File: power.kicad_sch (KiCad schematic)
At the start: 70 parts, among them U801 TPS566231P, U802 TPS566231P, U803 TPS566231P, U804 TPS566231P

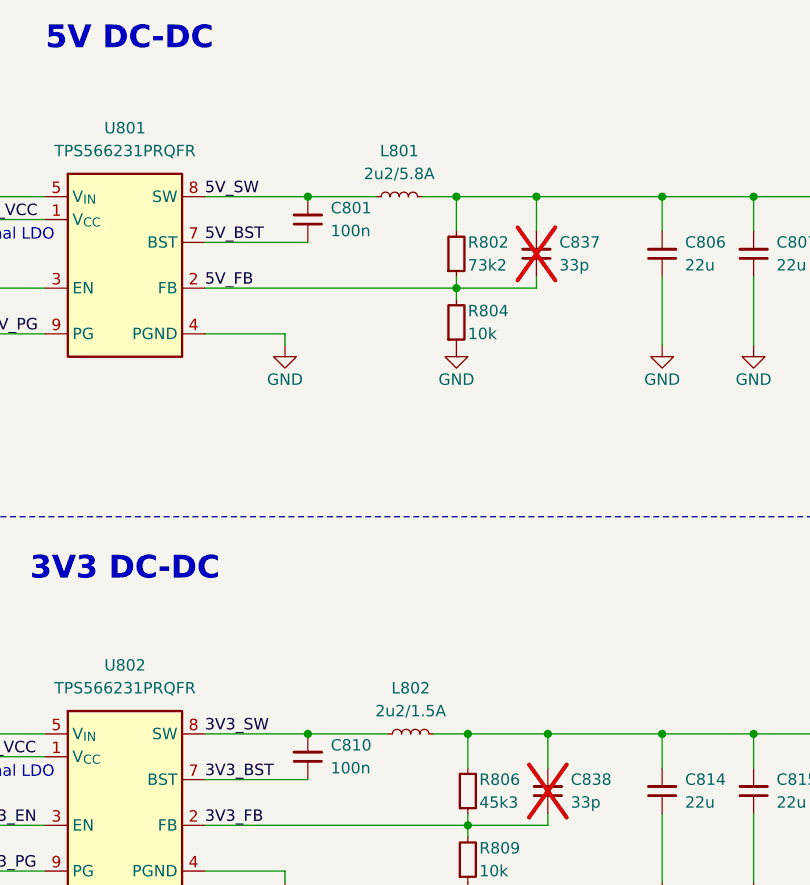
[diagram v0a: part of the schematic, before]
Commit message: [#100501] Change 5V & 3V3 DCDC inductors for SRP3212A-2R2M
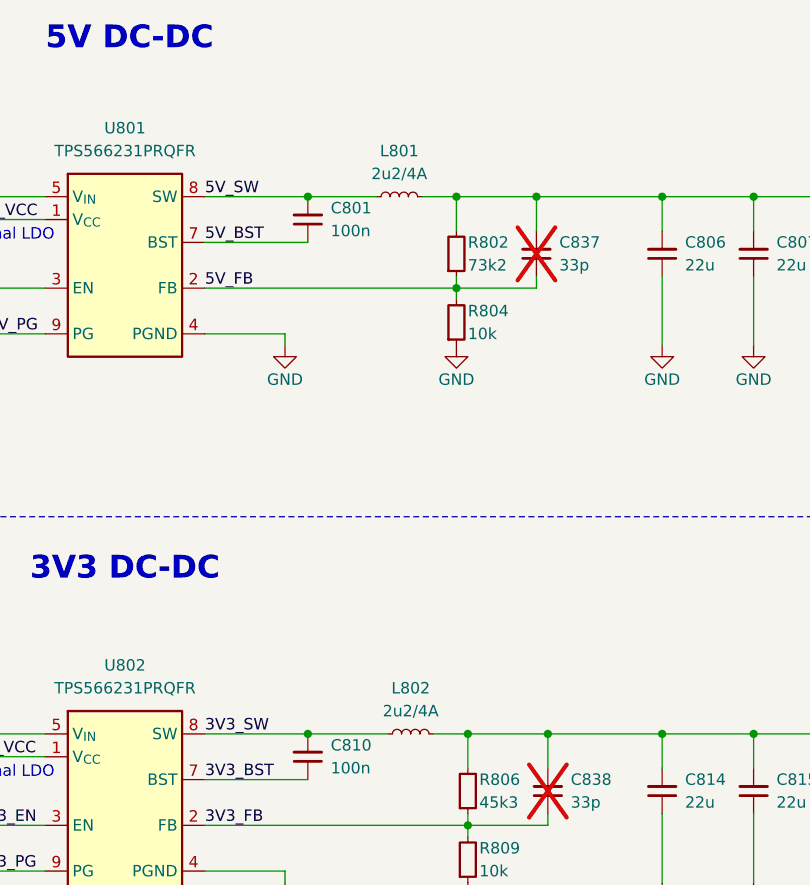
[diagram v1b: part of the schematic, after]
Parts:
- L801: value L_2u2_5.8A_WE-PMFI-35329222 -> L_2u2_4A_Bourns-SRP3212A; footprint antmicro-footprints:L_WE-PMFI-353220 -> antmicro-footprints:L_Bourns-SRP3212A; symbol antmicroFixedInductors:L_2u2_5.8A_WE-PMFI-35329222 -> antmicroFixedInductors:L_2u2_4A_Bourns-SRP3212A; IMax 5.8A -> 4 A; ISat 7.8A -> 4.8 A; MPN 74479335329222 -> SRP3212A-2R2M; Manufacturer Würth Elektronik -> Bourns; Size 3.5x3.2x2.0 -> 3.2x2.5; Val 2u2/5.8A -> 2u2/4A
- L802: value L_2u2_1.5A_0806 -> L_2u2_4A_Bourns-SRP3212A; footprint antmicro-footprints:L_0806_2016Metric -> antmicro-footprints:L_Bourns-SRP3212A; symbol antmicroFixedInductors:L_2u2_1.5A_0806 -> antmicroFixedInductors:L_2u2_4A_Bourns-SRP3212A; IMax (none) -> 4 A; ISat (none) -> 4.8 A; Imax 1.5A -> (none); Isat 1.2A -> (none); MPN 1285AS-H-2R2M=P2 -> SRP3212A-2R2M; Manufacturer Murata -> Bourns; Size 2.0x1.6 -> 3.2x2.5; Val 2u2/1.5A -> 2u2/4A
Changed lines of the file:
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@@
 	)
 	(symbol
-		(lib_id "antmicroFixedInductors:L_2u2_5.8A_WE-PMFI-35329222")
+		(lib_id "antmicroFixedInductors:L_2u2_4A_Bourns-SRP3212A")
 		(at 233.68 40.64 0)
 		(unit 1)
@@
 			)
 		)
-		(property "Value" "L_2u2_5.8A_WE-PMFI-35329222"
+		(property "Value" "L_2u2_4A_Bourns-SRP3212A"
 			(at 247.65 43.18 0)
 			(hide yes)
@@
 			)
 		)
-		(property "Footprint" "antmicro-footprints:L_WE-PMFI-353220"
+		(property "Footprint" "antmicro-footprints:L_Bourns-SRP3212A"
 			(at 247.65 48.26 0)
 			(hide yes)
@@
 			)
 		)
-		(property "Datasheet" "https://www.we-online.com/components/products/datasheet/74479335329222.pdf"
+		(property "Datasheet" "https://bourns.com/docs/product-datasheets/srp3212a.pdf?sfvrsn=7a275df6_6"
 			(at 247.65 50.8 0)
 			(hide yes)
@@
 			)
 		)
-		(property "Description" "Power Inductors - SMD WE-PMFI 2.2 uH 5.8 A 40 mOhms AEC-Q200"
+		(property "Description" "Power Inductor (SMD), 2.2 µH, 4 A, Shielded, 4.8 A, SRP3212 Series"
 			(at 247.65 71.12 0)
 			(hide yes)
@@
 			)
 		)
-		(property "Val" "2u2/5.8A"
+		(property "Val" "2u2/4A"
 			(at 236.22 38.1 0)
 			(show_name no)
@@
 			)
 		)
-		(property "Manufacturer" "Würth Elektronik"
+		(property "Manufacturer" "Bourns"
 			(at 247.65 53.34 0)
 			(hide yes)
@@
 			)
 		)
-		(property "MPN" "74479335329222"
+		(property "MPN" "SRP3212A-2R2M "
 			(at 247.65 55.88 0)
 			(hide yes)
@@
 			)
 		)
-		(property "ISat" "7.8A"
-			(at 247.65 58.42 0)
+		(property "ISat" "4.8 A"
+			(at 247.65 57.15 0)
 			(hide yes)
 			(show_name no)
@@
 					(size 1.27 1.27)
 				)
-				(justify left bottom)
+				(justify left)
 			)
 		)
-		(property "IMax" "5.8A"
+		(property "IMax" "4 A"
 			(at 247.65 60.96 0)
 			(hide yes)
@@
 			)
 		)
-		(property "Size" "3.5x3.2x2.0"
+		(property "Size" "3.2x2.5"
 			(at 247.65 63.5 0)
 			(hide yes)
@@
 	)
 	(symbol
-		(lib_id "antmicroFixedInductors:L_2u2_1.5A_0806")
+		(lib_id "antmicroFixedInductors:L_2u2_4A_Bourns-SRP3212A")
 		(at 234.95 100.33 0)
 		(unit 1)
@@
 			)
 		)
-		(property "Value" "L_2u2_1.5A_0806"
+		(property "Value" "L_2u2_4A_Bourns-SRP3212A"
 			(at 248.92 102.87 0)
 			(hide yes)
@@
 			)
 		)
-		(property "Footprint" "antmicro-footprints:L_0806_2016Metric"
+		(property "Footprint" "antmicro-footprints:L_Bourns-SRP3212A"
 			(at 248.92 107.95 0)
 			(hide yes)
@@
 			)
 		)
-		(property "Datasheet" "https://search.murata.co.jp/Ceramy/image/img/P02/J(E)TE243A-0011.pdf"
+		(property "Datasheet" "https://bourns.com/docs/product-datasheets/srp3212a.pdf?sfvrsn=7a275df6_6"
 			(at 248.92 110.49 0)
 			(hide yes)
@@
 			)
 		)
-		(property "Description" "Power Inductor (SMD), 2.2 µH, 1.2 A, Shielded, 1.5 A, DFE201610C"
+		(property "Description" "Power Inductor (SMD), 2.2 µH, 4 A, Shielded, 4.8 A, SRP3212 Series"
 			(at 248.92 130.81 0)
 			(hide yes)
@@
 			)
 		)
-		(property "Val" "2u2/1.5A"
+		(property "Val" "2u2/4A"
 			(at 237.49 97.79 0)
 			(show_name no)
@@
 				(font
 					(size 1.27 1.27)
+					(thickness 0.15)
 				)
 			)
 		)
-		(property "Manufacturer" "Murata"
+		(property "Manufacturer" "Bourns"
 			(at 248.92 113.03 0)
 			(hide yes)
@@
 				(font
 					(size 1.27 1.27)
+					(thickness 0.15)
 				)
 				(justify left bottom)
 			)
 		)
-		(property "MPN" "1285AS-H-2R2M=P2"
+		(property "MPN" "SRP3212A-2R2M "
 			(at 248.92 115.57 0)
 			(hide yes)
@@
 				(font
 					(size 1.27 1.27)
+					(thickness 0.15)
 				)
 				(justify left bottom)
 			)
 		)
-		(property "ISat" ""
+		(property "ISat" "4.8 A"
 			(at 248.92 116.84 0)
 			(hide yes)
@@
 			)
 		)
-		(property "Isat" "1.2A"
-			(at 248.92 118.11 0)
-			(hide yes)
-			(show_name no)
-			(do_not_autoplace no)
-			(effects
-				(font
-					(size 1.27 1.27)
-				)
-				(justify left bottom)
-			)
-		)
-		(property "IMax" ""
+		(property "IMax" "4 A"
 			(at 248.92 120.65 0)
 			(hide yes)
@@
 			)
 		)
-		(property "Imax" "1.5A"
-			(at 248.92 120.65 0)
-			(hide yes)
-			(show_name no)
-			(do_not_autoplace no)
-			(effects
-				(font
-					(size 1.27 1.27)
-				)
-				(justify left bottom)
-			)
-		)
-		(property "Size" "2.0x1.6"
+		(property "Size" "3.2x2.5"
 			(at 248.92 123.19 0)
 			(hide yes)
@@
 				(font
 					(size 1.27 1.27)
+					(thickness 0.15)
 				)
 				(justify left bottom)
@@
 				(font
 					(size 1.27 1.27)
+					(thickness 0.15)
 				)
 				(justify left bottom)
@@
 				(font
 					(size 1.27 1.27)
+					(thickness 0.15)
 				)
 				(justify left bottom)

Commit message: [#100501] Reannotate schematic
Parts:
- renumbered C801 to C29, C802 to C30, C803 to C31, C804 to C32, C805 to C33, C837 to C34, C806 to C35, C807 to C36, C808 to C37, C809 to C38, C810 to C39, C811 to C40, C812 to C41, C813 to C42, C838 to C43, C814 to C44, C815 to C45, C816 to C46, C817 to C47, C818 to C48, C819 to C49, C820 to C50, C821 to C51, C822 to C52, C839 to C53, C823 to C54, C824 to C55, C825 to C56, C826 to C57, C827 to C58, C828 to C59, C829 to C60, C830 to C61, C831 to C62, C832 to C63, C840 to C64, C833 to C65, C834 to C66, C835 to C67, C836 to C68, L801 to L1, L802 to L2, L803 to L3, L804 to L4, R801 to R73, R821 to R74, R803 to R75, R802 to R76, R822 to R77, R804 to R78, R805 to R79, R806 to R80, R807 to R81, R808 to R82, R809 to R83, R810 to R84, R811 to R85, R812 to R86, R813 to R87, R814 to R88, R815 to R89, R816 to R90, R817 to R91, R818 to R92, R819 to R93, R820 to R94, U801 to U4, U802 to U5, U803 to U6, U804 to U7

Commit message: [#100501] Correct +3V3_HPM_FRU connection
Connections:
- net +1V05: no longer R88.1
- net +3V3: now also R88.1

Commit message: [#100501] Change 1V2 and 1V05 DCDC inductors and add current draw assumptions
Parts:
- L3, L4: value L_2u2_1.5A_0806 -> L_1u_2.6A_0806; symbol antmicroFixedInductors:L_2u2_1.5A_0806 -> antmicroFixedInductors:L_1u_2.6A_0806; IMax (none) -> 2.6 A; ISat (none) -> 2.9 A; Imax 1.5A -> (none); Isat 1.2A -> (none); MPN 1285AS-H-2R2M=P2 -> SRP2010-1R0M; Manufacturer Murata -> Bourns; Val 2u2/1.5A -> 1u/2.6A
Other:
- note added: "1V05 @ 1A"
- note added: "1V2 @ 0.5A"
- note added: "3V3 @ 1A"
- note added: "5V @ 3.5A"
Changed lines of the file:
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@@
 		)
 	)
+	(text "3V3 @ 1A"
+		(exclude_from_sim no)
+		(at 267.462 97.536 0)
+		(effects
+			(font
+				(size 1.27 1.27)
+			)
+		)
+	)
+	(text "5V @ 3.5A"
+		(exclude_from_sim no)
+		(at 268.986 37.846 0)
+		(effects
+			(font
+				(size 1.27 1.27)
+			)
+		)
+	)
 	(text "V_{OUT} = 0.6 x (1 + R_{H}/R_{L}) [V]"
 		(exclude_from_sim no)
@@
 		)
 	)
+	(text "1V2 @ 0.5A"
+		(exclude_from_sim no)
+		(at 268.224 212.09 0)
+		(effects
+			(font
+				(size 1.27 1.27)
+			)
+		)
+	)
 	(text "1V05 DC-DC"
 		(exclude_from_sim no)
@@
 		)
 	)
+	(text "1V05 @ 1A"
+		(exclude_from_sim no)
+		(at 266.954 151.384 0)
+		(effects
+			(font
+				(size 1.27 1.27)
+			)
+		)
+	)
 	(text "VCC_SCM_HPM_FRU \n+3V3 +/- 5%\n0.627W"
 		(exclude_from_sim no)
@@
 	)
 	(symbol
-		(lib_id "antmicroFixedInductors:L_2u2_1.5A_0806")
+		(lib_id "antmicroFixedInductors:L_1u_2.6A_0806")
 		(at 237.49 214.63 0)
 		(unit 1)
@@
 			)
 		)
-		(property "Value" "L_2u2_1.5A_0806"
+		(property "Value" "L_1u_2.6A_0806"
 			(at 251.46 217.17 0)
 			(hide yes)
@@
 			)
 		)
-		(property "Datasheet" "https://search.murata.co.jp/Ceramy/image/img/P02/J(E)TE243A-0011.pdf"
+		(property "Datasheet" "https://www.bourns.com/docs/Product-Datasheets/SRP2010.pdf"
 			(at 251.46 224.79 0)
 			(hide yes)
@@
 			)
 		)
-		(property "Description" "Power Inductor (SMD), 2.2 µH, 1.2 A, Shielded, 1.5 A, DFE201610C"
+		(property "Description" "Wirewound Inductor, 1 µH, 0.072 ohm, 2.6 A, SRP2010"
 			(at 251.46 245.11 0)
 			(hide yes)
@@
 			)
 		)
-		(property "Val" "2u2/1.5A"
+		(property "Val" "1u/2.6A"
 			(at 240.03 212.09 0)
 			(show_name no)
@@
 				(font
 					(size 1.27 1.27)
+					(thickness 0.15)
 				)
 			)
 		)
-		(property "Manufacturer" "Murata"
+		(property "Manufacturer" "Bourns"
 			(at 251.46 227.33 0)
 			(hide yes)
@@
 				(font
 					(size 1.27 1.27)
+					(thickness 0.15)
 				)
 				(justify left bottom)
 			)
 		)
-		(property "MPN" "1285AS-H-2R2M=P2"
+		(property "MPN" "SRP2010-1R0M"
 			(at 251.46 229.87 0)
 			(hide yes)
@@
 				(font
 					(size 1.27 1.27)
+					(thickness 0.15)
 				)
 				(justify left bottom)
 			)
 		)
-		(property "ISat" ""
+		(property "ISat" "2.9 A"
 			(at 251.46 231.14 0)
 			(hide yes)
@@
 			)
 		)
-		(property "Isat" "1.2A"
-			(at 251.46 232.41 0)
-			(hide yes)
-			(show_name no)
-			(do_not_autoplace no)
-			(effects
-				(font
-					(size 1.27 1.27)
-				)
-				(justify left bottom)
-			)
-		)
-		(property "IMax" ""
+		(property "IMax" "2.6 A"
 			(at 251.46 234.95 0)
 			(hide yes)
@@
 			)
 		)
-		(property "Imax" "1.5A"
-			(at 251.46 234.95 0)
-			(hide yes)
-			(show_name no)
-			(do_not_autoplace no)
-			(effects
-				(font
-					(size 1.27 1.27)
-				)
-				(justify left bottom)
-			)
-		)
 		(property "Size" "2.0x1.6"
 			(at 251.46 237.49 0)
@@
 				(font
 					(size 1.27 1.27)
+					(thickness 0.15)
 				)
 				(justify left bottom)
@@
 				(font
 					(size 1.27 1.27)
+					(thickness 0.15)
 				)
 				(justify left bottom)
@@
 				(font
 					(size 1.27 1.27)
+					(thickness 0.15)
 				)
 				(justify left bottom)
@@
 	)
 	(symbol
-		(lib_id "antmicroFixedInductors:L_2u2_1.5A_0806")
+		(lib_id "antmicroFixedInductors:L_1u_2.6A_0806")
 		(at 237.49 153.67 0)
 		(unit 1)
@@
 			)
 		)
-		(property "Value" "L_2u2_1.5A_0806"
+		(property "Value" "L_1u_2.6A_0806"
 			(at 251.46 156.21 0)
 			(hide yes)
@@
 			)
 		)
-		(property "Datasheet" "https://search.murata.co.jp/Ceramy/image/img/P02/J(E)TE243A-0011.pdf"
+		(property "Datasheet" "https://www.bourns.com/docs/Product-Datasheets/SRP2010.pdf"
 			(at 251.46 163.83 0)
 			(hide yes)
@@
 			)
 		)
-		(property "Description" "Power Inductor (SMD), 2.2 µH, 1.2 A, Shielded, 1.5 A, DFE201610C"
+		(property "Description" "Wirewound Inductor, 1 µH, 0.072 ohm, 2.6 A, SRP2010"
 			(at 251.46 184.15 0)
 			(hide yes)
@@
 			)
 		)
-		(property "Val" "2u2/1.5A"
+		(property "Val" "1u/2.6A"
 			(at 240.03 151.13 0)
 			(show_name no)
@@
 				(font
 					(size 1.27 1.27)
+					(thickness 0.15)
 				)
 			)
 		)
-		(property "Manufacturer" "Murata"
+		(property "Manufacturer" "Bourns"
 			(at 251.46 166.37 0)
 			(hide yes)
@@
 				(font
 					(size 1.27 1.27)
+					(thickness 0.15)
 				)
 				(justify left bottom)
 			)
 		)
-		(property "MPN" "1285AS-H-2R2M=P2"
+		(property "MPN" "SRP2010-1R0M"
 			(at 251.46 168.91 0)
 			(hide yes)
@@
 				(font
 					(size 1.27 1.27)
+					(thickness 0.15)
 				)
 				(justify left bottom)
 			)
 		)
-		(property "ISat" ""
+		(property "ISat" "2.9 A"
 			(at 251.46 170.18 0)
 			(hide yes)
@@
 			)
 		)
-		(property "Isat" "1.2A"
-			(at 251.46 171.45 0)
-			(hide yes)
-			(show_name no)
-			(do_not_autoplace no)
-			(effects
-				(font
-					(size 1.27 1.27)
-				)
-				(justify left bottom)
-			)
-		)
-		(property "IMax" ""
+		(property "IMax" "2.6 A"
 			(at 251.46 173.99 0)
 			(hide yes)
@@
 			)
 		)
-		(property "Imax" "1.5A"
-			(at 251.46 173.99 0)
-			(hide yes)
-			(show_name no)
-			(do_not_autoplace no)
-			(effects
-				(font
-					(size 1.27 1.27)
-				)
-				(justify left bottom)
-			)
-		)
 		(property "Size" "2.0x1.6"
 			(at 251.46 176.53 0)
@@
 				(font
 					(size 1.27 1.27)
+					(thickness 0.15)
 				)
 				(justify left bottom)
@@
 				(font
 					(size 1.27 1.27)
+					(thickness 0.15)
 				)
 				(justify left bottom)
@@
 				(font
 					(size 1.27 1.27)
+					(thickness 0.15)
 				)
 				(justify left bottom)

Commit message: [#100501] Add test pints to DC-DC converters output and power indicator LEDs
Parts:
- added D19, D20, D21, D22: LED_G_0402_VLMTG1500-GS08, antmicro-footprints:LED_0402_1005Metric_G, symbol antmicroLEDIndicationDiscrete:LED_G_0402_VLMTG1500-GS08
- added Q8, Q9: DTC014T_SOT-416, antmicro-footprints:SOT-416, symbol antmicroTransistorsBipolarSingle:DTC014T_SOT-416
- added R156, R158, R159, R164: R_10k_0402, antmicro-footprints:R_0402_1005Metric, symbol antmicroResistors0402:R_10k_0402
- added TP20, TP21, TP22, TP35: TP_0.75mm_SMD, antmicro-footprints:TP_SMD_0.75mm, symbol antmicroTestPoints:TP_0.75mm_SMD
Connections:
- net GND: now also D21.1 (C), D22.1 (C), Q8.2 (E), Q9.2 (E)
- net +3V3_OUT: now reaches C43.2, C44.2, C45.2, C46.2, C47.2, L2.2, R79.1, R80.2
- net +3V3_OUT: now also R156.2, R158.2, R164.2, TP22.1
- net +1V2_OUT: now reaches C64.2, C65.2, C66.2, C67.2, C68.2, L4.2, R90.1, R91.2
- net +1V2_OUT: now also Q9.1 (B), TP21.1
- net +5V0_OUT: now reaches C34.2, C35.2, C36.2, C37.2, C38.2, L1.2, R73.1, R76.2
- net +5V0_OUT: now also R159.2, TP35.1
- net +1V05_OUT: now reaches C53.2, C54.2, C55.2, C56.2, C57.2, L3.2, R84.1, R85.2
- net +1V05_OUT: now also Q8.1 (B), TP20.1
- new net: D22.2 (A), R164.1
- new net: D19.1 (C), Q8.3 (C)
- new net: D21.2 (A), R159.1
- new net: D19.2 (A), R156.1
- new net: D20.1 (C), Q9.3 (C)
- new net: D20.2 (A), R158.1
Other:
- note removed: "-->"
- note removed: "1V2"
- note removed: "3V3 & 1V05"
- note removed: "5V"
- moved on the sheet: C34, C35, C36, C37, C38, C43, C44, C45, C46, C47, C53, C54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

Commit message: [#100501] Reannotate schematic
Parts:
- renumbered C29 to C33, C30 to C35, C31 to C36, C32 to C37, C33 to C38, C35 to C39, C36 to C40, C37 to C41, C38 to C42, C39 to C43, C43 to C44, C40 to C45, C41 to C46, C42 to C47, C44 to C49, C45 to C50, C46 to C51, C47 to C52, C49 to C53, C53 to C54, C50 to C55, C51 to C56, C52 to C57, C54 to C59, C55 to C60, C56 to C61, C57 to C62, C59 to C63, C60 to C65, C61 to C66, C62 to C67, C63 to C68, C65 to C69, C66 to C70, C67 to C71, C68 to C72, D19 to D1, D20 to D2, D21 to D3, D22 to D4, Q8 to Q1, Q9 to Q2, R73 to R103, R74 to R104, R76 to R105, R75 to R106, R77 to R107, R78 to R108, R79 to R109, R80 to R110, R81 to R111, R82 to R112, R88 to R113, R83 to R114, R84 to R115, R85 to R116, R86 to R117, R87 to R118, R89 to R119, R90 to R120, R91 to R121, R92 to R122, R93 to R123, R94 to R124, R159 to R125, R164 to R126, R156 to R127, R158 to R128, TP35 to TP3, TP22 to TP4, TP20 to TP5, TP21 to TP6, U4 to U3, U5 to U4, U6 to U5, U7 to U6

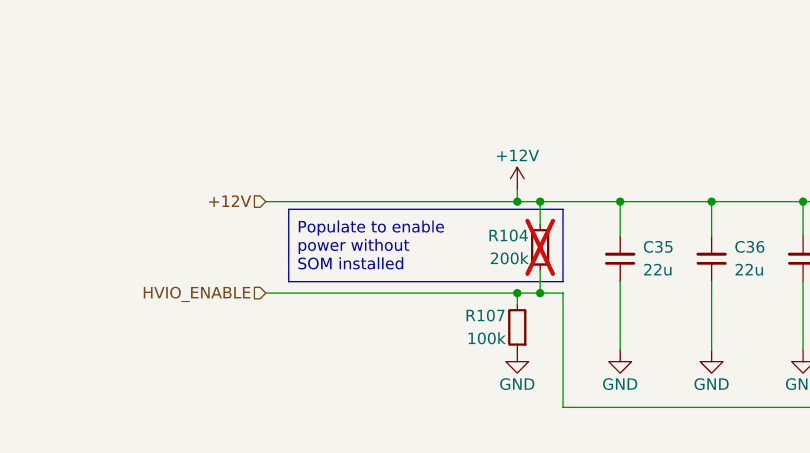
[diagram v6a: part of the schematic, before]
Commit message: [#100501] Add test points to 12V, 1V8 and 1V1 rails
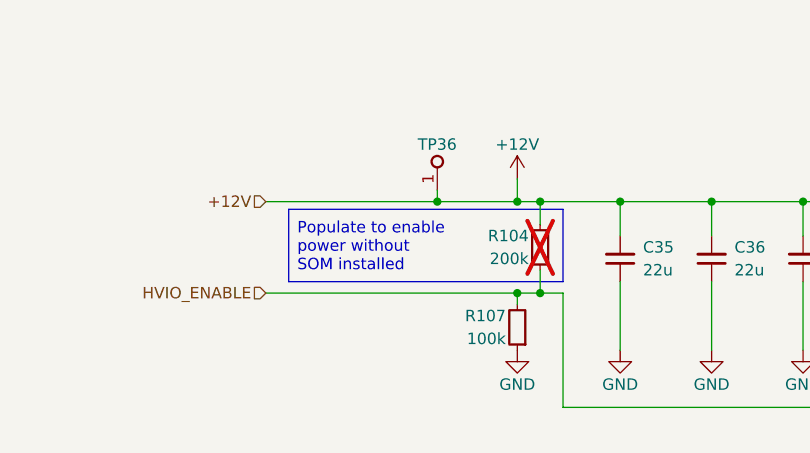
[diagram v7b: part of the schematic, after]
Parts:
- added TP36: TP_0.75mm_SMD, antmicro-footprints:TP_SMD_0.75mm, symbol antmicroTestPoints:TP_0.75mm_SMD
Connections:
- net +12V: now also TP36.1
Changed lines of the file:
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@@
 	)
 	(junction
+		(at 107.95 40.64)
+		(diameter 0)
+		(color 0 0 0 0)
+	)
+	(junction
 		(at 325.12 100.33)
 		(diameter 0)
@@
 	(wire
 		(pts
-			(xy 88.9 40.64) (xy 119.38 40.64)
+			(xy 88.9 40.64) (xy 116.84 40.64)
+		)
+		(stroke
+			(width 0)
+			(type default)
+		)
+	)
+	(wire
+		(pts
+			(xy 116.84 40.64) (xy 119.38 40.64)
 		)
 		(stroke
@@
 	(wire
 		(pts
+			(xy 107.95 39.37) (xy 107.95 40.64)
+		)
+		(stroke
+			(width 0)
+			(type default)
+		)
+	)
+	(wire
+		(pts
 			(xy 171.45 217.17) (xy 171.45 222.25)
 		)
@@
 	(wire
 		(pts
-			(xy 116.84 39.37) (xy 116.84 40.64)
+			(xy 116.84 38.1) (xy 116.84 40.64)
 		)
 		(stroke
@@
 	)
 	(symbol
+		(lib_id "antmicroTestPoints:TP_0.75mm_SMD")
+		(at 107.95 39.37 90)
+		(unit 1)
+		(body_style 1)
+		(exclude_from_sim no)
+		(in_bom no)
+		(on_board yes)
+		(in_pos_files yes)
+		(dnp no)
+		(property "Reference" "TP36"
+			(at 107.95 34.29 90)
+			(show_name no)
+			(do_not_autoplace no)
+			(effects
+				(font
+					(size 1.27 1.27)
+					(thickness 0.15)
+				)
+			)
+		)
+		(property "Value" "TP_0.75mm_SMD"
+			(at 111.76 29.21 0)
+			(hide yes)
+			(show_name no)
+			(do_not_autoplace no)
+			(effects
+				(font
+					(size 1.27 1.27)
+					(thickness 0.15)
+				)
+				(justify left bottom)
+			)
+		)
+		(property "Footprint" "antmicro-footprints:TP_SMD_0.75mm"
+			(at 114.3 29.21 0)
+			(hide yes)
+			(show_name no)
+			(do_not_autoplace no)
+			(effects
+				(font
+					(size 1.27 1.27)
+					(thickness 0.15)
+				)
+				(justify left bottom)
+			)
+		)
+		(property "Datasheet" ""
+			(at 120.65 21.59 0)
+			(hide yes)
+			(show_name no)
+			(do_not_autoplace no)
+			(effects
+				(font
+					(size 1.27 1.27)
+					(thickness 0.15)
+				)
+				(justify left bottom)
+			)
+		)
+		(property "Description" "SMT test point"
+			(at 121.92 28.575 0)
+			(hide yes)
+			(show_name no)
+			(do_not_autoplace no)
+			(effects
+				(font
+					(size 1.27 1.27)
+				)
+				(justify left bottom)
+			)
+		)
+		(property "MPN" ""
+			(at 119.38 28.575 0)
+			(hide yes)
+			(show_name no)
+			(do_not_autoplace no)
+			(effects
+				(font
+					(size 1.27 1.27)
+					(thickness 0.15)
+				)
+				(justify left bottom)
+			)
+		)
+		(property "Manufacturer" ""
+			(at 114.3 28.575 0)
+			(hide yes)
+			(show_name no)
+			(do_not_autoplace no)
+			(effects
+				(font
+					(size 1.27 1.27)
+					(thickness 0.15)
+				)
+				(justify left bottom)
+			)
+		)
+		(property "Author" "Antmicro"
+			(at 116.84 29.21 0)
+			(hide yes)
+			(show_name no)
+			(do_not_autoplace no)
+			(effects
+				(font
+					(size 1.27 1.27)
+					(thickness 0.15)
+				)
+				(justify left bottom)
+			)
+		)
+		(property "License" "Apache-2.0"
+			(at 119.38 29.21 0)
+			(hide yes)
+			(show_name no)
+			(do_not_autoplace no)
+			(effects
+				(font
+					(size 1.27 1.27)
+					(thickness 0.15)
+				)
+				(justify left bottom)
+			)
+		)
+		(pin "1"
+		)
+		(instances
+			(project "altera-modular-agilex-5-dc-scm"
+				(path "/6bb9d978-a328-4b30-874b-55170a976185/ec2bc394-f073-4549-a45a-609fd3c852aa"
+					(reference "TP36")
+					(unit 1)
+				)
+			)
+		)
+	)
+	(symbol
 		(lib_id "antmicroCapacitors0603:C_22u_16V_0603")
 		(at 265.43 52.07 90)
@@
 	(symbol
 		(lib_id "antmicropower:+12V")
-		(at 116.84 39.37 0)
+		(at 116.84 38.1 0)
 		(unit 1)
 		(body_style 1)
@@
 		(dnp no)
 		(property "Reference" "#PWR052"
-			(at 116.84 43.18 0)
+			(at 116.84 41.91 0)
 			(hide yes)
 			(show_name no)
@@
 		)
 		(property "Value" "+12V"
-			(at 116.84 35.56 0)
+			(at 116.84 34.29 0)
 			(show_name no)
 			(do_not_autoplace no)
@@
 		)
 		(property "Footprint" ""
-			(at 116.84 39.37 0)
+			(at 116.84 38.1 0)
 			(hide yes)
 			(show_name no)
@@
 		)
 		(property "Datasheet" ""
-			(at 116.84 39.37 0)
+			(at 116.84 38.1 0)
 			(hide yes)
 			(show_name no)
@@
 		)
 		(property "Description" ""
-			(at 116.84 45.72 0)
+			(at 116.84 44.45 0)
 			(hide yes)
 			(show_name no)
